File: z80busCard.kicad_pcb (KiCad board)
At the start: 2 copper layers, 4 parts, among them J1 Conn_02x20_Odd_Even, J2 Conn_02x20_Odd_Even, J3 Conn_02x20_Odd_Even, J4 Conn_02x20_Odd_Even

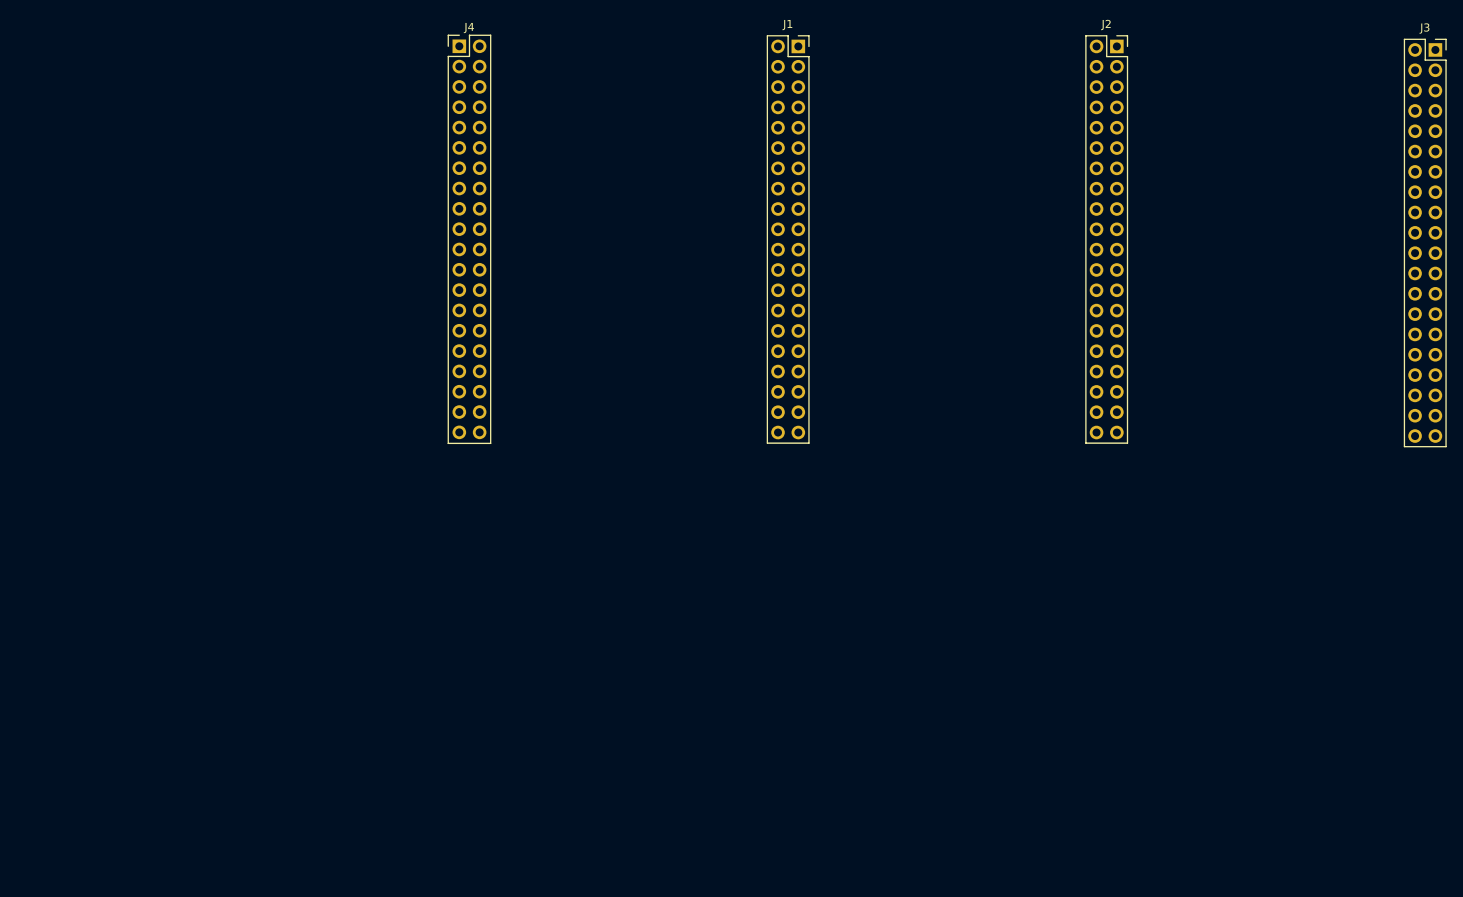
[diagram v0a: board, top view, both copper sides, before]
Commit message: Added reset circuit
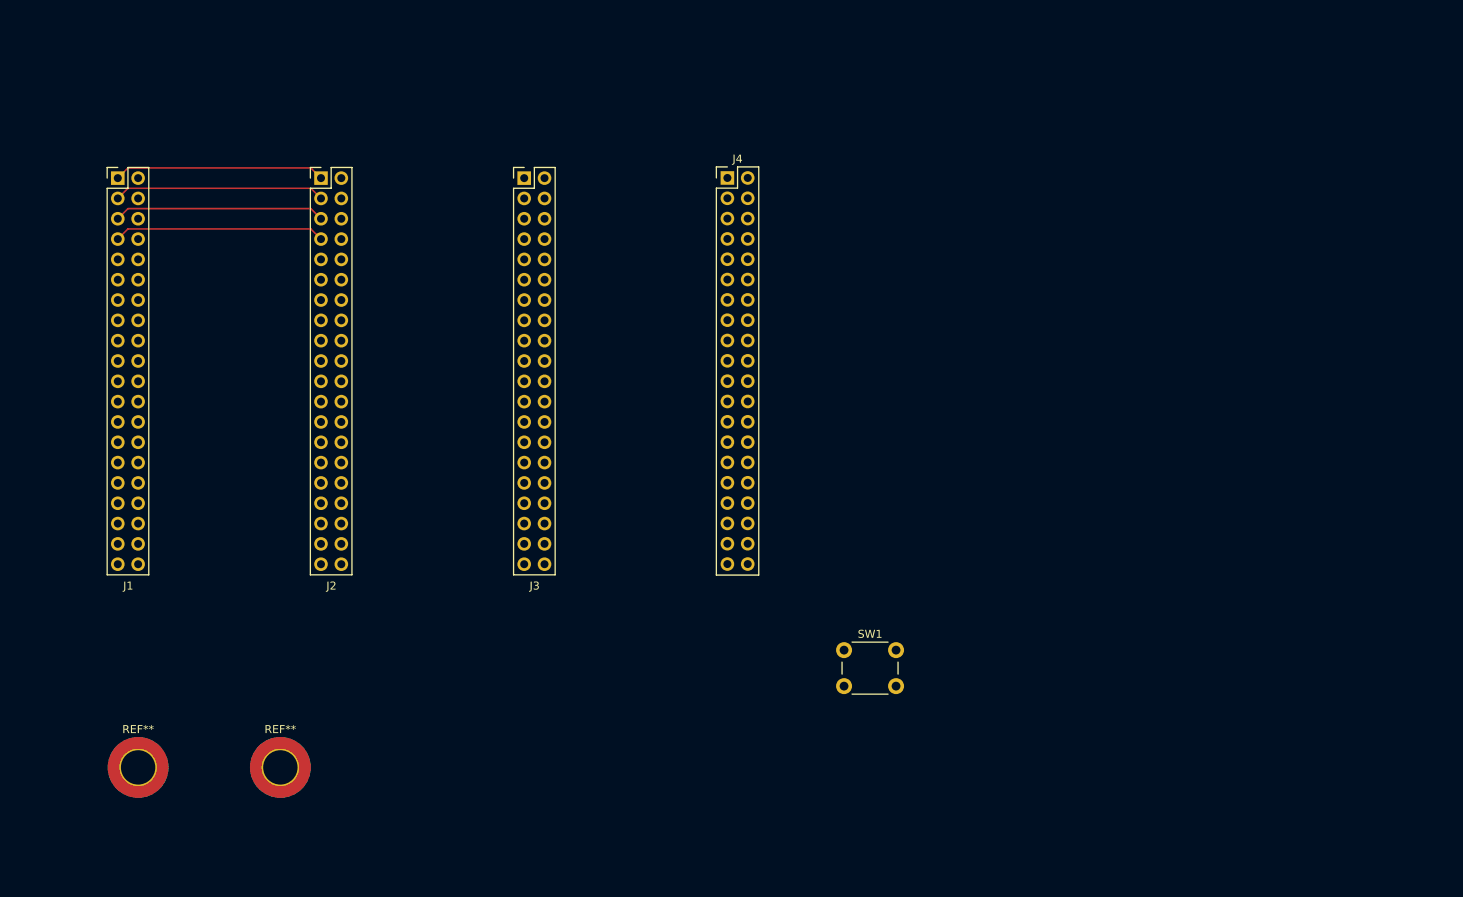
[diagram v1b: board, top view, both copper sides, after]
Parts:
- added REF**: MountingHole_4.3mm_M4_ISO7380_Pad_TopBottom, MountingHole:MountingHole_4.3mm_M4_ISO7380_Pad_TopBottom, F.Cu at (53.3, 149.9)
- added REF**: MountingHole_4.3mm_M4_ISO7380_Pad_TopBottom, MountingHole:MountingHole_4.3mm_M4_ISO7380_Pad_TopBottom, F.Cu at (71.1, 149.9)
- added SW1: SW_Push, Button_Switch_THT:SW_PUSH_6mm_H4.3mm, F.Cu at (141.6, 135.2)
- J1, J2, J3: footprint Connector_PinSocket_2.54mm:PinSocket_2x20_P2.54mm_Vertical -> Library:PinSocket_2x20_P2.54mm_Vertical_Mirrored
- moved J3 112.5 mm to (104.2, 76.2)
- moved J2 98.3 mm to (78.8, 76.2)
- moved J1 84.1 mm to (53.4, 76.2)
- moved J4 37.3 mm to (127.0, 76.2)
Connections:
- J1 pad 1: unconnected-(J1-Pin_1-Pad1) -> /A12
- J1 pad 11: unconnected-(J1-Pin_11-Pad11) -> /~{M1}
- J1 pad 13: unconnected-(J1-Pin_13-Pad13) -> /~{MREQ}
- J1 pad 15: unconnected-(J1-Pin_15-Pad15) -> /~{IOREQ}
- J1 pad 17: unconnected-(J1-Pin_17-Pad17) -> /~{RD}
- J1 pad 19: unconnected-(J1-Pin_19-Pad19) -> /{WR}
- J1 pad 21: unconnected-(J1-Pin_21-Pad21) -> /~{WAIT}
- J1 pad 23: unconnected-(J1-Pin_23-Pad23) -> /~{INT}
- J1 pad 25: unconnected-(J1-Pin_25-Pad25) -> /~{CLK}
- J1 pad 27: unconnected-(J1-Pin_27-Pad27) -> /~{RESET}
- J1 pad 29: unconnected-(J1-Pin_29-Pad29) -> /~{BUSREQ}
- J1 pad 3: unconnected-(J1-Pin_3-Pad3) -> /A13
- J1 pad 31: unconnected-(J1-Pin_31-Pad31) -> /~{BUSACK}
- J1 pad 33: unconnected-(J1-Pin_33-Pad33) -> +5V
- J1 pad 35: unconnected-(J1-Pin_35-Pad35) -> /~{CE_1}
- J1 pad 37: unconnected-(J1-Pin_37-Pad37) -> /~{CE_2}
- J1 pad 39: unconnected-(J1-Pin_39-Pad39) -> /~{CE_3}
- J1 pad 5: unconnected-(J1-Pin_5-Pad5) -> /A14
- J1 pad 7: unconnected-(J1-Pin_7-Pad7) -> /A15
- J1 pad 9: unconnected-(J1-Pin_9-Pad9) -> GND
- J2 pad 1: unconnected-(J2-Pin_1-Pad1) -> /A12
- J2 pad 11: unconnected-(J2-Pin_11-Pad11) -> /~{M1}
- J2 pad 13: unconnected-(J2-Pin_13-Pad13) -> /~{MREQ}
- J2 pad 15: unconnected-(J2-Pin_15-Pad15) -> /~{IOREQ}
- J2 pad 17: unconnected-(J2-Pin_17-Pad17) -> /~{RD}
- J2 pad 19: unconnected-(J2-Pin_19-Pad19) -> /{WR}
- J2 pad 21: unconnected-(J2-Pin_21-Pad21) -> /~{WAIT}
- J2 pad 23: unconnected-(J2-Pin_23-Pad23) -> /~{INT}
- J2 pad 25: unconnected-(J2-Pin_25-Pad25) -> /~{CLK}
- J2 pad 27: unconnected-(J2-Pin_27-Pad27) -> /~{RESET}
- J2 pad 29: unconnected-(J2-Pin_29-Pad29) -> /~{BUSREQ}
- J2 pad 3: unconnected-(J2-Pin_3-Pad3) -> /A13
- J2 pad 31: unconnected-(J2-Pin_31-Pad31) -> /~{BUSACK}
- J2 pad 33: unconnected-(J2-Pin_33-Pad33) -> +5V
- J2 pad 35: unconnected-(J2-Pin_35-Pad35) -> /~{CE_1}
- J2 pad 37: unconnected-(J2-Pin_37-Pad37) -> /~{CE_2}
- J2 pad 39: unconnected-(J2-Pin_39-Pad39) -> /~{CE_3}
- J2 pad 5: unconnected-(J2-Pin_5-Pad5) -> /A14
- J2 pad 7: unconnected-(J2-Pin_7-Pad7) -> /A15
- J2 pad 9: unconnected-(J2-Pin_9-Pad9) -> GND
- J3 pad 1: unconnected-(J3-Pin_1-Pad1) -> /A12
- J3 pad 11: unconnected-(J3-Pin_11-Pad11) -> /~{M1}
- J3 pad 13: unconnected-(J3-Pin_13-Pad13) -> /~{MREQ}
- J3 pad 15: unconnected-(J3-Pin_15-Pad15) -> /~{IOREQ}
- J3 pad 17: unconnected-(J3-Pin_17-Pad17) -> /~{RD}
- J3 pad 19: unconnected-(J3-Pin_19-Pad19) -> /{WR}
- J3 pad 21: unconnected-(J3-Pin_21-Pad21) -> /~{WAIT}
- J3 pad 23: unconnected-(J3-Pin_23-Pad23) -> /~{INT}
- J3 pad 25: unconnected-(J3-Pin_25-Pad25) -> /~{CLK}
- J3 pad 27: unconnected-(J3-Pin_27-Pad27) -> /~{RESET}
- J3 pad 29: unconnected-(J3-Pin_29-Pad29) -> /~{BUSREQ}
- J3 pad 3: unconnected-(J3-Pin_3-Pad3) -> /A13
- J3 pad 31: unconnected-(J3-Pin_31-Pad31) -> /~{BUSACK}
- J3 pad 33: unconnected-(J3-Pin_33-Pad33) -> +5V
- J3 pad 35: unconnected-(J3-Pin_35-Pad35) -> /~{CE_1}
- J3 pad 37: unconnected-(J3-Pin_37-Pad37) -> /~{CE_2}
- J3 pad 39: unconnected-(J3-Pin_39-Pad39) -> /~{CE_3}
- J3 pad 5: unconnected-(J3-Pin_5-Pad5) -> /A14
- J3 pad 7: unconnected-(J3-Pin_7-Pad7) -> /A15
- J3 pad 9: unconnected-(J3-Pin_9-Pad9) -> GND
- J4 pad 1: unconnected-(J4-Pin_1-Pad1) -> /A12
- J4 pad 11: unconnected-(J4-Pin_11-Pad11) -> /~{M1}
- J4 pad 13: unconnected-(J4-Pin_13-Pad13) -> /~{MREQ}
- J4 pad 15: unconnected-(J4-Pin_15-Pad15) -> /~{IOREQ}
- J4 pad 17: unconnected-(J4-Pin_17-Pad17) -> /~{RD}
- J4 pad 19: unconnected-(J4-Pin_19-Pad19) -> /{WR}
- J4 pad 21: unconnected-(J4-Pin_21-Pad21) -> /~{WAIT}
- J4 pad 23: unconnected-(J4-Pin_23-Pad23) -> /~{INT}
- J4 pad 25: unconnected-(J4-Pin_25-Pad25) -> /~{CLK}
- J4 pad 27: unconnected-(J4-Pin_27-Pad27) -> /~{RESET}
- J4 pad 29: unconnected-(J4-Pin_29-Pad29) -> /~{BUSREQ}
- J4 pad 3: unconnected-(J4-Pin_3-Pad3) -> /A13
- J4 pad 31: unconnected-(J4-Pin_31-Pad31) -> /~{BUSACK}
- J4 pad 33: unconnected-(J4-Pin_33-Pad33) -> +5V
- J4 pad 35: unconnected-(J4-Pin_35-Pad35) -> /~{CE_1}
- J4 pad 37: unconnected-(J4-Pin_37-Pad37) -> /~{CE_2}
- J4 pad 39: unconnected-(J4-Pin_39-Pad39) -> /~{CE_3}
- J4 pad 5: unconnected-(J4-Pin_5-Pad5) -> /A14
- J4 pad 7: unconnected-(J4-Pin_7-Pad7) -> /A15
- J4 pad 9: unconnected-(J4-Pin_9-Pad9) -> GND
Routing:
- net /A15: track 0.00 -> 26.5 mm
- net /A14: track 0.00 -> 26.5 mm
- net /A13: track 0.00 -> 26.5 mm
- net /A12: track 0.00 -> 26.5 mm

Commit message: Wired front layer. Added silkscreen labels
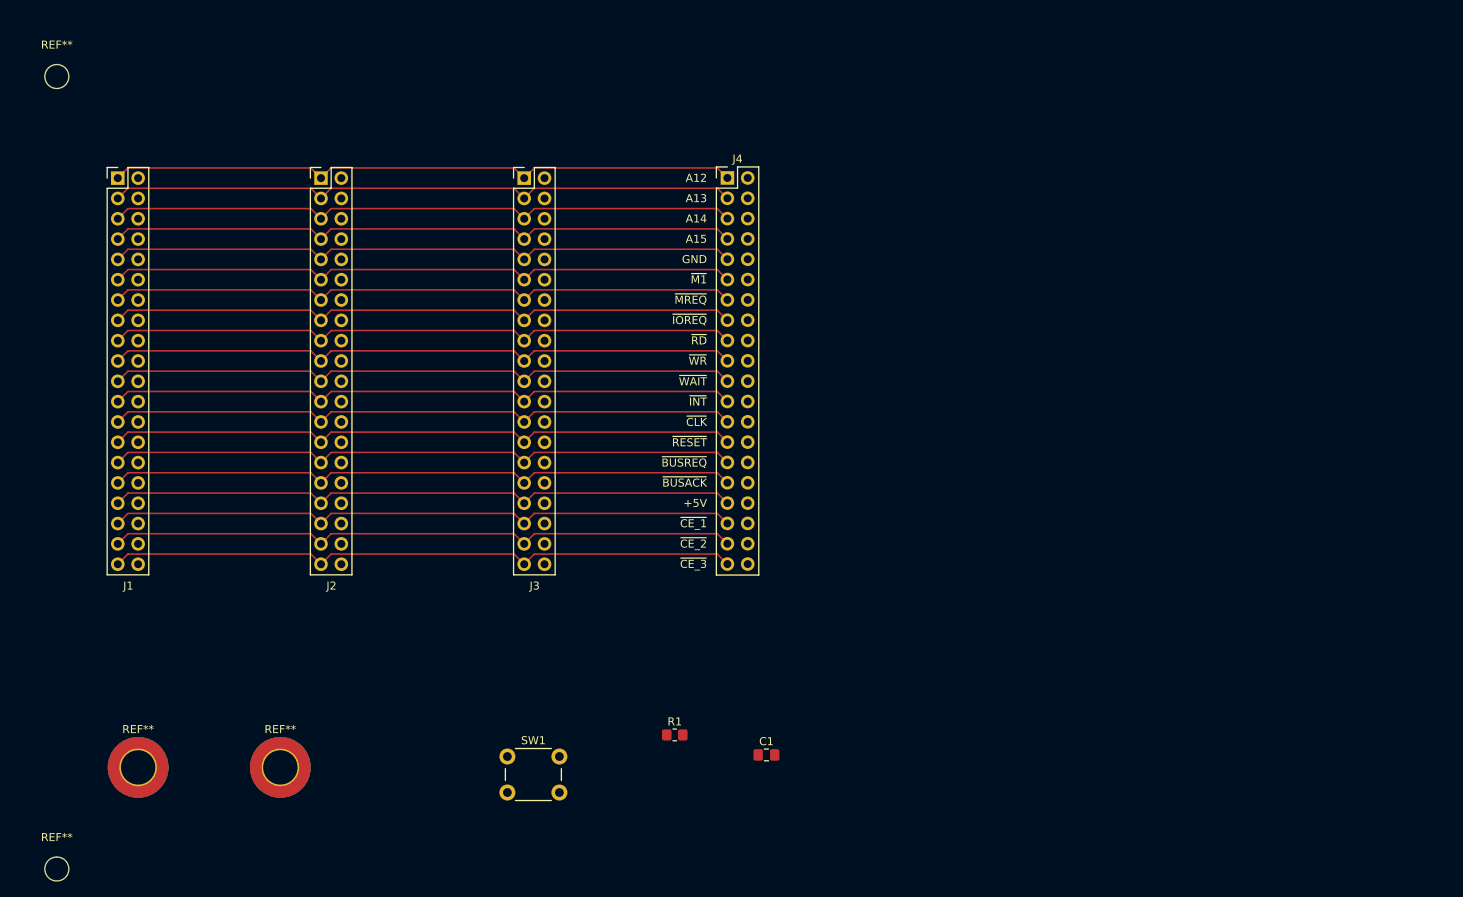
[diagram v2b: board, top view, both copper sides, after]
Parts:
- added C1: 10u, Capacitor_SMD:C_0805_2012Metric_Pad1.18x1.45mm_HandSolder, F.Cu at (131.9, 148.3)
- added R1: 10k, Resistor_SMD:R_0805_2012Metric_Pad1.20x1.40mm_HandSolder, F.Cu at (120.4, 145.8)
- added REF**: MountingHole_3mm, MountingHole:MountingHole_3mm, F.Cu at (43.2, 162.6)
- added REF**: MountingHole_3mm, MountingHole:MountingHole_3mm, F.Cu at (43.2, 63.5)
- moved SW1 44.1 mm to (99.5, 148.5)
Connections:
- net /{WR} renamed /~{WR}
- SW1 pad 1: unconnected-(SW1-Pad1) -> GND
- SW1 pad 2: unconnected-(SW1-Pad2) -> /~{RESET}
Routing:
- net /~{IOREQ}: track 0.00 -> 79.4 mm
- net /~{CLK}: track 0.00 -> 79.4 mm
- net /~{M1}: track 0.00 -> 79.4 mm
- net /~{BUSREQ}: track 0.00 -> 79.4 mm
- net +5V: track 0.00 -> 79.4 mm
- net GND: track 0.00 -> 79.4 mm
- net /~{INT}: track 0.00 -> 79.4 mm
- net /~{WR}: track 0.00 -> 79.4 mm
- net /~{WAIT}: track 0.00 -> 79.4 mm
- net /~{RESET}: track 0.00 -> 79.4 mm
- net /~{RD}: track 0.00 -> 79.4 mm
- net /~{MREQ}: track 0.00 -> 79.4 mm
- net /~{CE_3}: track 0.00 -> 79.4 mm
- net /~{CE_2}: track 0.00 -> 79.4 mm
- net /~{CE_1}: track 0.00 -> 79.4 mm
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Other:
- board text added: "+5V"
- board text added: "A12"
- board text added: "A13"
- board text added: "A14"
- board text added: "A15"
- board text added: "GND"
- board text added: "~{BUSACK}"
- board text added: "~{BUSREQ}"
- board text added: "~{CE_1}"
- board text added: "~{CE_2}"
- board text added: "~{CE_3}"
- board text added: "~{CLK}"
- board text added: "~{INT}"
- board text added: "~{IOREQ}"
- board text added: "~{M1}"
- board text added: "~{MREQ}"
- board text added: "~{RD}"
- board text added: "~{RESET}"
- board text added: "~{WAIT}"
- board text added: "~{WR}"

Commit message: Completed for order
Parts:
- added J5: USB_C_Receptacle_PowerOnly_6P, Connector_USB:USB_C_Receptacle_GCT_USB4125-xx-x_6P_TopMnt_Horizontal, F.Cu at (99.6, 134.6)
- added REF**: MountingHole_3mm, MountingHole:MountingHole_3mm, F.Cu at (148.6, 67.3)
- added REF**: MountingHole_3mm, MountingHole:MountingHole_3mm, F.Cu at (148.6, 135.9)
- moved GND 98.9 mm to (143.5, 109.2), turned to 90 degrees
- moved +5V 93.0 mm to (143.5, 91.4), turned to 90 degrees
- moved SW1 52.5 mm to (147.8, 127.9), turned to 180 degrees
- moved R1 39.0 mm to (147.8, 118.1), turned to 180 degrees
- moved REF** 26.7 mm to (43.2, 135.9)
- moved C1 23.4 mm to (137.3, 125.5), turned to -90 degrees
- moved REF** 3.81 mm to (43.2, 67.3)
- renumbered REF** to +5V, REF** to GND
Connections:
- +5V pad 1: (no net) -> +5V
- GND pad 1: (no net) -> GND
- J1 pad 10: unconnected-(J1-Pin_10-Pad10) -> /D4
- J1 pad 12: unconnected-(J1-Pin_12-Pad12) -> /D5
- J1 pad 14: unconnected-(J1-Pin_14-Pad14) -> /D6
- J1 pad 16: unconnected-(J1-Pin_16-Pad16) -> /D7
- J1 pad 18: unconnected-(J1-Pin_18-Pad18) -> /A0
- J1 pad 2: unconnected-(J1-Pin_2-Pad2) -> /D0
- J1 pad 20: unconnected-(J1-Pin_20-Pad20) -> /A1
- J1 pad 22: unconnected-(J1-Pin_22-Pad22) -> /A2
- J1 pad 24: unconnected-(J1-Pin_24-Pad24) -> /A3
- J1 pad 26: unconnected-(J1-Pin_26-Pad26) -> /A4
- J1 pad 28: unconnected-(J1-Pin_28-Pad28) -> /A5
- J1 pad 30: unconnected-(J1-Pin_30-Pad30) -> /A6
- J1 pad 32: unconnected-(J1-Pin_32-Pad32) -> /A7
- J1 pad 34: unconnected-(J1-Pin_34-Pad34) -> /A8
- J1 pad 36: unconnected-(J1-Pin_36-Pad36) -> /A9
- J1 pad 38: unconnected-(J1-Pin_38-Pad38) -> /A10
- J1 pad 4: unconnected-(J1-Pin_4-Pad4) -> /D1
- J1 pad 40: unconnected-(J1-Pin_40-Pad40) -> /A11
- J1 pad 6: unconnected-(J1-Pin_6-Pad6) -> /D2
- J1 pad 8: unconnected-(J1-Pin_8-Pad8) -> /D3
- J2 pad 10: unconnected-(J2-Pin_10-Pad10) -> /D4
- J2 pad 12: unconnected-(J2-Pin_12-Pad12) -> /D5
- J2 pad 14: unconnected-(J2-Pin_14-Pad14) -> /D6
- J2 pad 16: unconnected-(J2-Pin_16-Pad16) -> /D7
- J2 pad 18: unconnected-(J2-Pin_18-Pad18) -> /A0
- J2 pad 2: unconnected-(J2-Pin_2-Pad2) -> /D0
- J2 pad 20: unconnected-(J2-Pin_20-Pad20) -> /A1
- J2 pad 22: unconnected-(J2-Pin_22-Pad22) -> /A2
- J2 pad 24: unconnected-(J2-Pin_24-Pad24) -> /A3
- J2 pad 26: unconnected-(J2-Pin_26-Pad26) -> /A4
- J2 pad 28: unconnected-(J2-Pin_28-Pad28) -> /A5
- J2 pad 30: unconnected-(J2-Pin_30-Pad30) -> /A6
- J2 pad 32: unconnected-(J2-Pin_32-Pad32) -> /A7
- J2 pad 34: unconnected-(J2-Pin_34-Pad34) -> /A8
- J2 pad 36: unconnected-(J2-Pin_36-Pad36) -> /A9
- J2 pad 38: unconnected-(J2-Pin_38-Pad38) -> /A10
- J2 pad 4: unconnected-(J2-Pin_4-Pad4) -> /D1
- J2 pad 40: unconnected-(J2-Pin_40-Pad40) -> /A11
- J2 pad 6: unconnected-(J2-Pin_6-Pad6) -> /D2
- J2 pad 8: unconnected-(J2-Pin_8-Pad8) -> /D3
- J3 pad 10: unconnected-(J3-Pin_10-Pad10) -> /D4
- J3 pad 12: unconnected-(J3-Pin_12-Pad12) -> /D5
- J3 pad 14: unconnected-(J3-Pin_14-Pad14) -> /D6
- J3 pad 16: unconnected-(J3-Pin_16-Pad16) -> /D7
- J3 pad 18: unconnected-(J3-Pin_18-Pad18) -> /A0
- J3 pad 2: unconnected-(J3-Pin_2-Pad2) -> /D0
- J3 pad 20: unconnected-(J3-Pin_20-Pad20) -> /A1
- J3 pad 22: unconnected-(J3-Pin_22-Pad22) -> /A2
- J3 pad 24: unconnected-(J3-Pin_24-Pad24) -> /A3
- J3 pad 26: unconnected-(J3-Pin_26-Pad26) -> /A4
- J3 pad 28: unconnected-(J3-Pin_28-Pad28) -> /A5
- J3 pad 30: unconnected-(J3-Pin_30-Pad30) -> /A6
- J3 pad 32: unconnected-(J3-Pin_32-Pad32) -> /A7
- J3 pad 34: unconnected-(J3-Pin_34-Pad34) -> /A8
- J3 pad 36: unconnected-(J3-Pin_36-Pad36) -> /A9
- J3 pad 38: unconnected-(J3-Pin_38-Pad38) -> /A10
- J3 pad 4: unconnected-(J3-Pin_4-Pad4) -> /D1
- J3 pad 40: unconnected-(J3-Pin_40-Pad40) -> /A11
- J3 pad 6: unconnected-(J3-Pin_6-Pad6) -> /D2
- J3 pad 8: unconnected-(J3-Pin_8-Pad8) -> /D3
- J4 pad 10: unconnected-(J4-Pin_10-Pad10) -> /D4
- J4 pad 12: unconnected-(J4-Pin_12-Pad12) -> /D5
- J4 pad 14: unconnected-(J4-Pin_14-Pad14) -> /D6
- J4 pad 16: unconnected-(J4-Pin_16-Pad16) -> /D7
- J4 pad 18: unconnected-(J4-Pin_18-Pad18) -> /A0
- J4 pad 2: unconnected-(J4-Pin_2-Pad2) -> /D0
- J4 pad 20: unconnected-(J4-Pin_20-Pad20) -> /A1
- J4 pad 22: unconnected-(J4-Pin_22-Pad22) -> /A2
- J4 pad 24: unconnected-(J4-Pin_24-Pad24) -> /A3
- J4 pad 26: unconnected-(J4-Pin_26-Pad26) -> /A4
- J4 pad 28: unconnected-(J4-Pin_28-Pad28) -> /A5
- J4 pad 30: unconnected-(J4-Pin_30-Pad30) -> /A6
- J4 pad 32: unconnected-(J4-Pin_32-Pad32) -> /A7
- J4 pad 34: unconnected-(J4-Pin_34-Pad34) -> /A8
- J4 pad 36: unconnected-(J4-Pin_36-Pad36) -> /A9
- J4 pad 38: unconnected-(J4-Pin_38-Pad38) -> /A10
- J4 pad 4: unconnected-(J4-Pin_4-Pad4) -> /D1
- J4 pad 40: unconnected-(J4-Pin_40-Pad40) -> /A11
- J4 pad 6: unconnected-(J4-Pin_6-Pad6) -> /D2
- J4 pad 8: unconnected-(J4-Pin_8-Pad8) -> /D3
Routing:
- net GND: track 79.4 -> 245.9 mm, vias 0 -> 3
- net +5V: track 79.4 -> 196.2 mm
- net /D1: track 0.00 -> 79.4 mm
- net /A9: track 0.00 -> 79.4 mm
- net /A2: track 0.00 -> 79.4 mm
- net /A0: track 0.00 -> 79.4 mm
- net /D3: track 0.00 -> 79.4 mm
- net /A11: track 0.00 -> 79.4 mm
- net /D6: track 0.00 -> 79.4 mm
- net /D4: track 0.00 -> 79.4 mm
- net /D0: track 0.00 -> 79.4 mm
- net /A8: track 0.00 -> 79.4 mm
- net /A6: track 0.00 -> 79.4 mm
- net /A5: track 0.00 -> 79.4 mm
- net /A4: track 0.00 -> 79.4 mm
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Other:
- board outline added: 115.6 x 78.7 mm
- board text added: "1"
- board text added: "2"
- board text added: "39"
- board text added: "40"
- board text added: "A0"
- board text added: "A1"
- board text added: "A10"
- board text added: "A11"
- board text added: "A2"
- board text added: "A3"
- board text added: "A4"
- board text added: "A5"
- board text added: "A6"
- board text added: "A7"
- board text added: "A8"
- board text added: "A9"
- board text added: "D0"
- board text added: "D1"
- board text added: "D2"
- board text added: "D3"
- board text added: "D4"
- board text added: "D5"
- board text added: "D6"
- board text added: "D7"
- board text added: "Z80 bus card v1 2025-10-05"
